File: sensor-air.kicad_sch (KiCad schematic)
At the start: 0 parts

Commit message: Adding I2C bus to circuit
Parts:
- added J7: Conn_02x04_Odd_Even, symbol Connector_Generic:Conn_02x04_Odd_Even
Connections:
- new net I2C.SCL: J7.6 (Pin_6)
- new net I2C.SDA: J7.8 (Pin_8)
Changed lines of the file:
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@@
 	(generator_version "8.0")
 	(paper "A4")
+	(bus_entry
+		(at 193.04 97.79)
+		(size 2.54 2.54)
+		(stroke
+			(width 0)
+			(type default)
+		)
+	)
+	(bus_entry
+		(at 193.04 100.33)
+		(size 2.54 2.54)
+		(stroke
+			(width 0)
+			(type default)
+		)
+	)
+	(wire
+		(pts
+			(xy 170.18 100.33) (xy 193.04 100.33)
+		)
+		(stroke
+			(width 0)
+			(type default)
+		)
+	)
+	(wire
+		(pts
+			(xy 170.18 97.79) (xy 193.04 97.79)
+		)
+		(stroke
+			(width 0)
+			(type default)
+		)
+	)
+	(bus
+		(pts
+			(xy 195.58 102.87) (xy 195.58 106.68)
+		)
+		(stroke
+			(width 0)
+			(type default)
+		)
+	)
+	(bus
+		(pts
+			(xy 195.58 106.68) (xy 214.63 106.68)
+		)
+		(stroke
+			(width 0)
+			(type default)
+		)
+	)
+	(bus
+		(pts
+			(xy 195.58 100.33) (xy 195.58 102.87)
+		)
+		(stroke
+			(width 0)
+			(type default)
+		)
+	)
+	(label "I2C.SCL"
+		(at 180.34 97.79 0)
+		(fields_autoplaced yes)
+		(effects
+			(font
+				(size 1.27 1.27)
+			)
+			(justify left bottom)
+		)
+	)
+	(label "I2C.SDA"
+		(at 180.34 100.33 0)
+		(fields_autoplaced yes)
+		(effects
+			(font
+				(size 1.27 1.27)
+			)
+			(justify left bottom)
+		)
+	)
+	(hierarchical_label "I2C{SCL SDA}"
+		(shape bidirectional)
+		(at 214.63 106.68 0)
+		(fields_autoplaced yes)
+		(effects
+			(font
+				(size 1.27 1.27)
+			)
+			(justify left)
+		)
+	)
+	(symbol
+		(lib_id "Connector_Generic:Conn_02x04_Odd_Even")
+		(at 162.56 95.25 0)
+		(unit 1)
+		(exclude_from_sim no)
+		(in_bom yes)
+		(on_board yes)
+		(dnp no)
+		(fields_autoplaced yes)
+		(property "Reference" "J7"
+			(at 163.83 86.36 0)
+			(effects
+				(font
+					(size 1.27 1.27)
+				)
+			)
+		)
+		(property "Value" "Conn_02x04_Odd_Even"
+			(at 163.83 88.9 0)
+			(effects
+				(font
+					(size 1.27 1.27)
+				)
+			)
+		)
+		(property "Footprint" ""
+			(at 162.56 95.25 0)
+			(effects
+				(font
+					(size 1.27 1.27)
+				)
+				(hide yes)
+			)
+		)
+		(property "Datasheet" "~"
+			(at 162.56 95.25 0)
+			(effects
+				(font
+					(size 1.27 1.27)
+				)
+				(hide yes)
+			)
+		)
+		(property "Description" "Generic connector, double row, 02x04, odd/even pin numbering scheme (row 1 odd numbers, row 2 even numbers), script generated (kicad-library-utils/schlib/autogen/connector/)"
+			(at 162.56 95.25 0)
+			(effects
+				(font
+					(size 1.27 1.27)
+				)
+				(hide yes)
+			)
+		)
+		(pin "3"
+		)
+		(pin "1"
+		)
+		(pin "5"
+		)
+		(pin "8"
+		)
+		(pin "7"
+		)
+		(pin "4"
+		)
+		(pin "2"
+		)
+		(pin "6"
+		)
+		(instances
+			(project ""
+				(path "/1c59de6a-87fe-4223-8898-4b0383164a31/51e979ab-bea6-4c65-a749-9f40ad447381"
+					(reference "J7")
+					(unit 1)
+				)
+			)
+		)
+	)
 )

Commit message: Adding symbols information
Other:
- company: (none) -> catbranchman
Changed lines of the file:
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@@
 	(generator_version "8.0")
 	(paper "A4")
+	(title_block
+		(company "catbranchman")
+		(comment 1 "Electrical Engineering Department")
+		(comment 2 "EE 156 / Stanford University")
+		(comment 3 "Flight Club, W6YX, Endurance")
+	)
 	(bus_entry
 		(at 193.04 97.79)

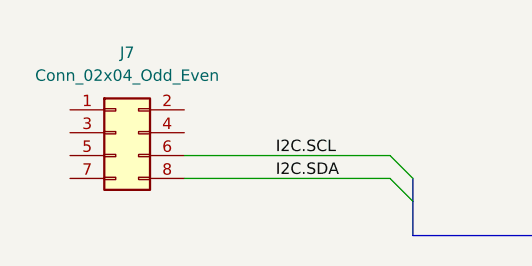
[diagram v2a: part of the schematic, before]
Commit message: Adding rest of schematic
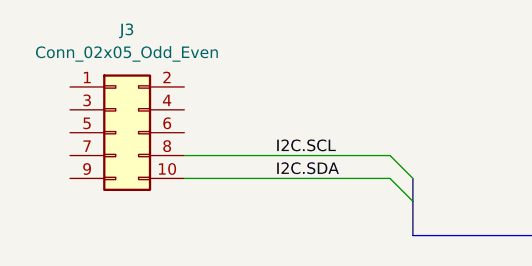
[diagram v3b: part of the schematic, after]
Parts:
- removed J7: Conn_02x04_Odd_Even, symbol Connector_Generic:Conn_02x04_Odd_Even
- added J3: Conn_02x05_Odd_Even, Connector_PinHeader_1.27mm:PinHeader_2x05_P1.27mm_Vertical_SMD, symbol Connector_Generic:Conn_02x05_Odd_Even
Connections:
- net I2C.SCL: now also J3.8 (Pin_8)
- net I2C.SDA: now also J3.10 (Pin_10)
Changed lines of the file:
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@@
 	)
 	(symbol
-		(lib_id "Connector_Generic:Conn_02x04_Odd_Even")
+		(lib_id "Connector_Generic:Conn_02x05_Odd_Even")
 		(at 162.56 95.25 0)
 		(unit 1)
@@
 		(dnp no)
 		(fields_autoplaced yes)
-		(property "Reference" "J7"
+		(property "Reference" "J3"
+			(at 163.83 83.82 0)
+			(effects
+				(font
+					(size 1.27 1.27)
+				)
+			)
+		)
+		(property "Value" "Conn_02x05_Odd_Even"
 			(at 163.83 86.36 0)
 			(effects
@@
 			)
 		)
-		(property "Value" "Conn_02x04_Odd_Even"
-			(at 163.83 88.9 0)
-			(effects
-				(font
-					(size 1.27 1.27)
-				)
-			)
-		)
-		(property "Footprint" ""
+		(property "Footprint" "Connector_PinHeader_1.27mm:PinHeader_2x05_P1.27mm_Vertical_SMD"
 			(at 162.56 95.25 0)
 			(effects
@@
 			)
 		)
-		(property "Datasheet" "~"
+		(property "Datasheet" "https://www.fischerelektronik.de/web_fischer/en_GB/VA/BLM2SMD10Z/datasheet.xhtml"
 			(at 162.56 95.25 0)
 			(effects
@@
 			)
 		)
-		(property "Description" "Generic connector, double row, 02x04, odd/even pin numbering scheme (row 1 odd numbers, row 2 even numbers), script generated (kicad-library-utils/schlib/autogen/connector/)"
+		(property "Description" "Generic connector, double row, 02x05, odd/even pin numbering scheme (row 1 odd numbers, row 2 even numbers), script generated (kicad-library-utils/schlib/autogen/connector/)"
 			(at 162.56 95.25 0)
 			(effects
@@
 			)
 		)
-		(pin "3"
+		(property "Mfr" "Fischer Elektronik"
+			(at 162.56 95.25 0)
+			(effects
+				(font
+					(size 1.27 1.27)
+				)
+				(hide yes)
+			)
 		)
-		(pin "1"
+		(property "Mfr P/N" "BLM 2 SMD 10 Z"
+			(at 162.56 95.25 0)
+			(effects
+				(font
+					(size 1.27 1.27)
+				)
+				(hide yes)
+			)
+		)
+		(property "Supplier_1" "Digikey"
+			(at 162.56 95.25 0)
+			(effects
+				(font
+					(size 1.27 1.27)
+				)
+				(hide yes)
+			)
+		)
+		(property "Supplier_1 P/N" "5496-BLM2SMD10Z-ND"
+			(at 162.56 95.25 0)
+			(effects
+				(font
+					(size 1.27 1.27)
+				)
+				(hide yes)
+			)
+		)
+		(property "Supplier_1 Unit Price" "$0.93000 "
+			(at 162.56 95.25 0)
+			(effects
+				(font
+					(size 1.27 1.27)
+				)
+				(hide yes)
+			)
+		)
+		(property "Supplier_1 Price @ Qty" ""
+			(at 162.56 95.25 0)
+			(effects
+				(font
+					(size 1.27 1.27)
+				)
+				(hide yes)
+			)
+		)
+		(property "Supplier_2" ""
+			(at 162.56 95.25 0)
+			(effects
+				(font
+					(size 1.27 1.27)
+				)
+				(hide yes)
+			)
+		)
+		(property "Supplier_2 P/N" ""
+			(at 162.56 95.25 0)
+			(effects
+				(font
+					(size 1.27 1.27)
+				)
+				(hide yes)
+			)
+		)
+		(property "Supplier_2 Unit Price" ""
+			(at 162.56 95.25 0)
+			(effects
+				(font
+					(size 1.27 1.27)
+				)
+				(hide yes)
+			)
+		)
+		(property "Supplier_2 Price @ Qty" ""
+			(at 162.56 95.25 0)
+			(effects
+				(font
+					(size 1.27 1.27)
+				)
+				(hide yes)
+			)
 		)
 		(pin "5"
+		)
+		(pin "4"
+		)
+		(pin "9"
+		)
+		(pin "3"
 		)
 		(pin "8"
@@
 		(pin "7"
 		)
-		(pin "4"
+		(pin "6"
+		)
+		(pin "1"
 		)
 		(pin "2"
 		)
-		(pin "6"
+		(pin "10"
 		)
 		(instances
 			(project ""
 				(path "/1c59de6a-87fe-4223-8898-4b0383164a31/51e979ab-bea6-4c65-a749-9f40ad447381"
-					(reference "J7")
+					(reference "J3")
 					(unit 1)
 				)

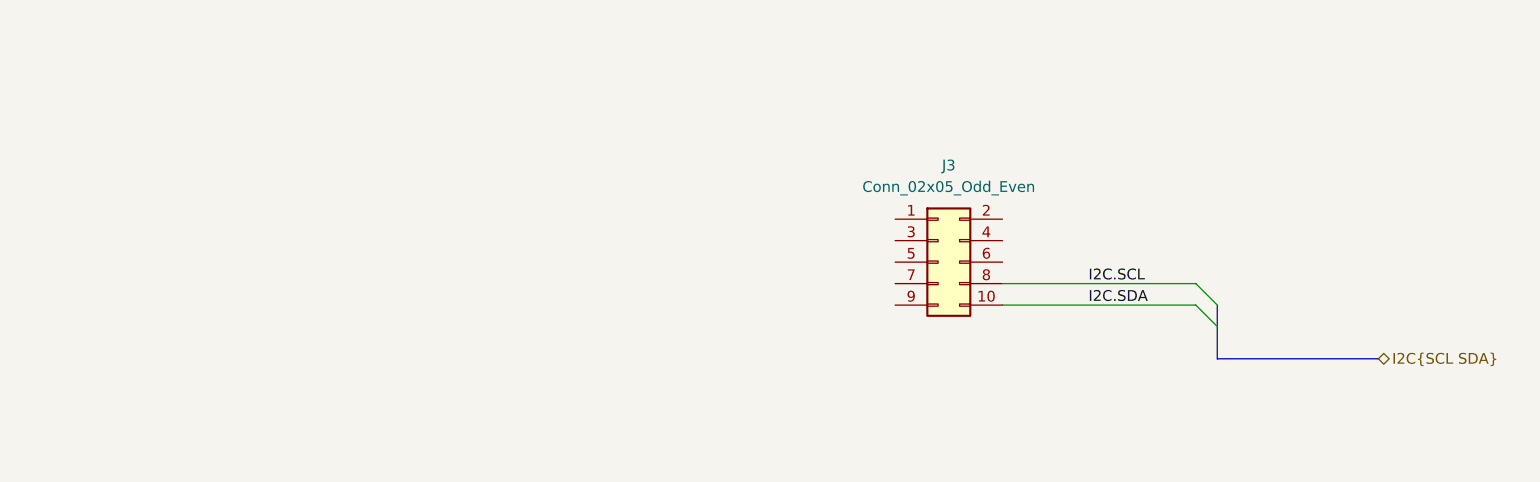
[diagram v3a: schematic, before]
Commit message: Spamming 0 ohm resistors
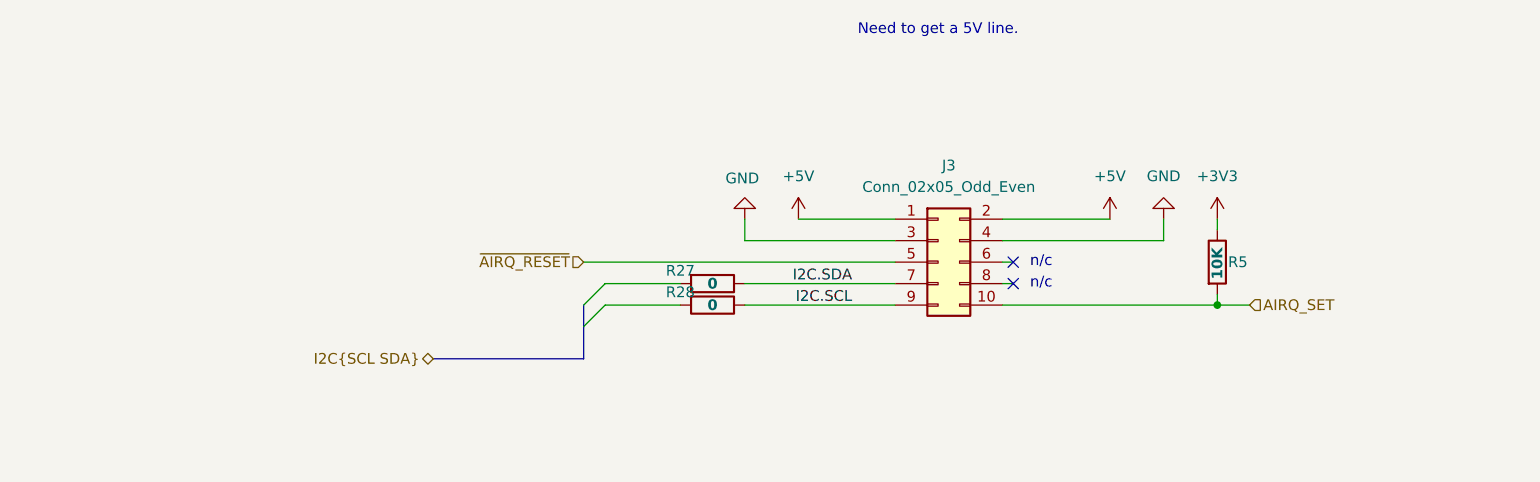
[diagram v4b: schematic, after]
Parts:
- added R27, R28: 0, Resistor_SMD:R_0603_1608Metric, symbol Device:R
- added R5: 10K, Resistor_SMD:R_0603_1608Metric, symbol Device:R
- J3: Mfr Fischer Elektronik -> Amphenol ICC (FCI); Mfr P/N BLM 2 SMD 10 Z -> 20021321-00010C4LF; Supplier_1 P/N 5496-BLM2SMD10Z-ND -> 609-3706-1-ND; Supplier_1 Price @ Qty (none) -> $0.79120; Supplier_1 Unit Price $0.93000 -> $1.35000
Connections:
- net I2C.SCL: now also J3.9 (Pin_9), R28.1; no longer J3.8 (Pin_8)
- net I2C.SDA: now also J3.7 (Pin_7), R27.1; no longer J3.10 (Pin_10)
- net +5V: now reaches J3.1 (Pin_1)
- net +5V: now also J3.2 (Pin_2)
- net GND: now reaches J3.3 (Pin_3)
- net GND: now also J3.4 (Pin_4)
- net ~{AIRQ_RESET}: now reaches J3.5 (Pin_5)
- new net +3V3: R5.1
- new net AIRQ_SET: J3.10 (Pin_10), R5.2
- no-connect marks 0 -> 2
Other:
- note added: "Need to get a 5V line."
- note added: "n/c"
- title: (none) -> Sensor - Air Quality

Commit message: Adding more 0 ohm resistors and pullups for I2C lines
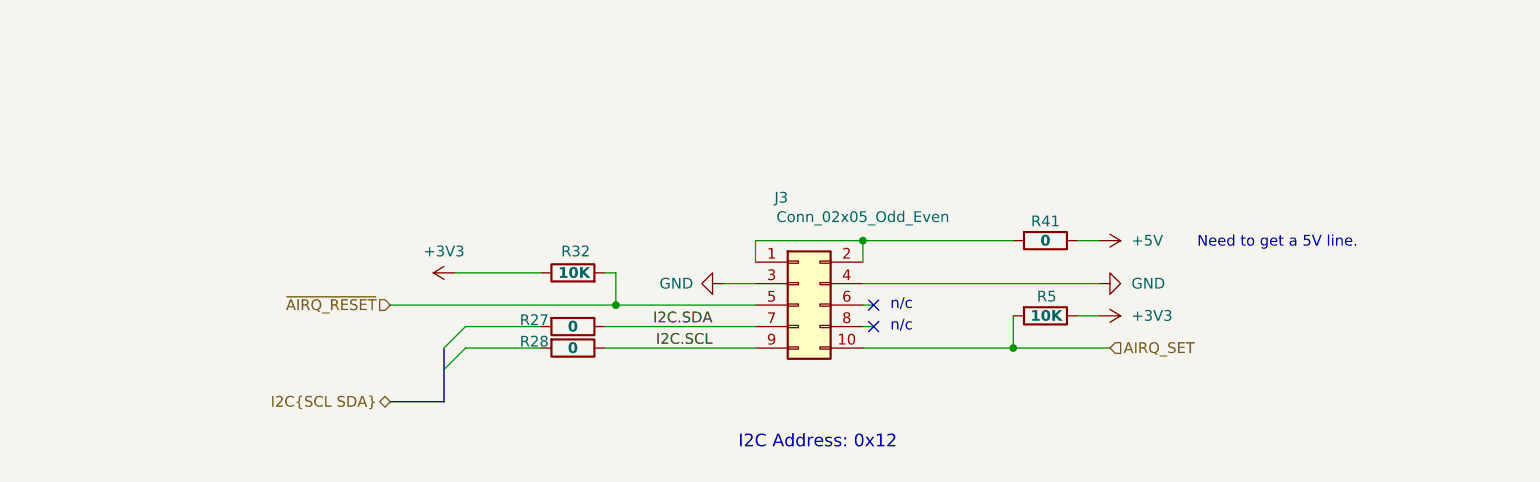
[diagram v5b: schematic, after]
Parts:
- added R32: 10K, Resistor_SMD:R_0603_1608Metric, symbol Device:R
- added R41: 0, Resistor_SMD:R_0603_1608Metric, symbol Device:R
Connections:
- net +3V3: now also R32.1
- net +5V: now also R41.1; no longer J3.1 (Pin_1), J3.2 (Pin_2)
- net ~{AIRQ_RESET}: now also R32.2
- new net: J3.1 (Pin_1), J3.2 (Pin_2), R41.2
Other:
- note added: "I2C Address: 0x12"
- moved on the sheet: J3, R27, R28, R5

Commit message: Adding diodes for Air Quality Sensor SET and RESET pins
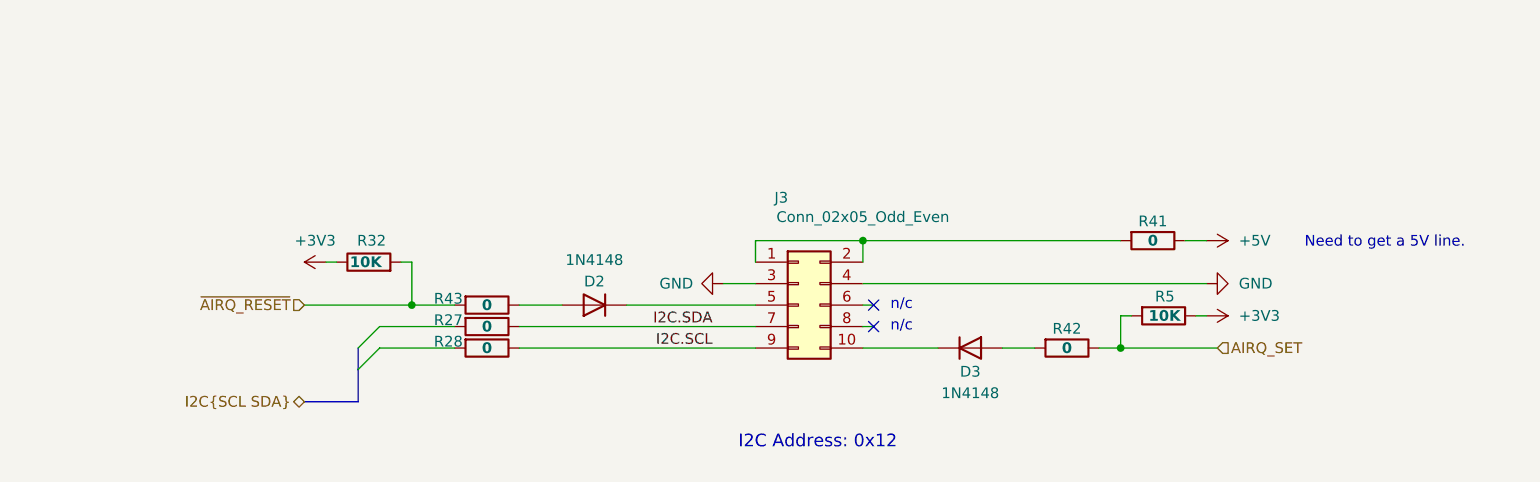
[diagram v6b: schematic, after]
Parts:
- added D2, D3: 1N4148, Diode_SMD:D_SOD-323F, symbol Device:D
- added R42, R43: 0, Resistor_SMD:R_0603_1608Metric, symbol Device:R
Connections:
- net AIRQ_SET: now also R42.1; no longer J3.10 (Pin_10)
- net ~{AIRQ_RESET}: now also R43.2; no longer J3.5 (Pin_5)
- new net: D2.2 (A), R43.1
- new net: D3.1 (K), J3.10 (Pin_10)
- new net: D3.2 (A), R42.2
- new net: D2.1 (K), J3.5 (Pin_5)
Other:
- moved on the sheet: R27, R28, R32, R41, R5

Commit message: Adding testpoints to I2C, SPI, and signals
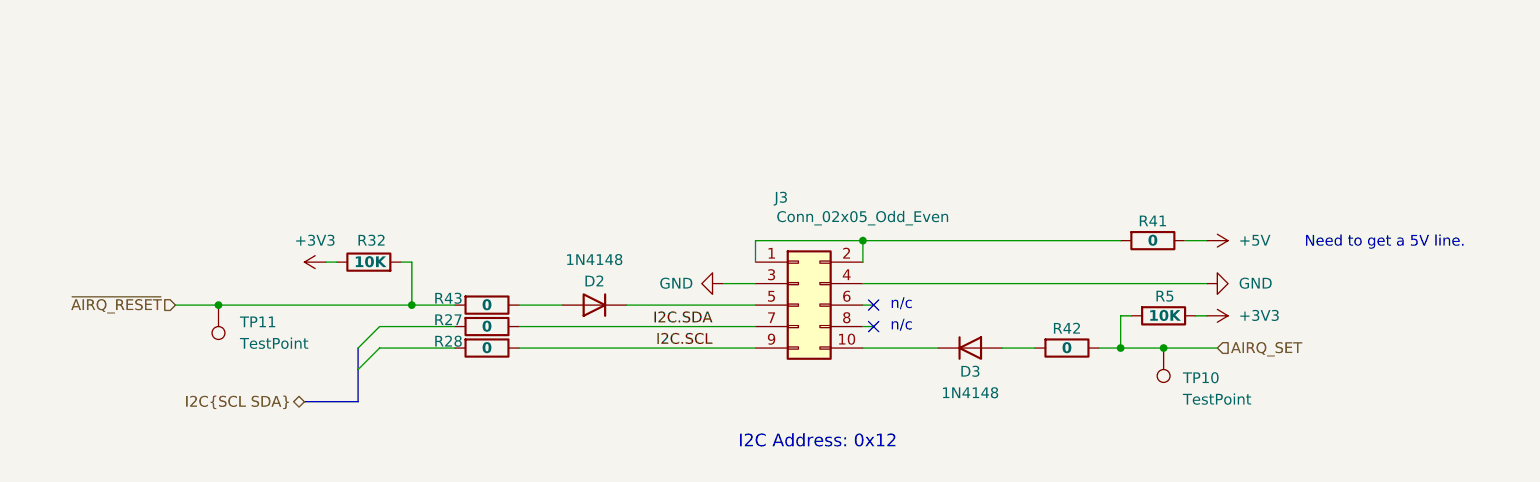
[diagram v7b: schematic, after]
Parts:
- added TP10, TP11: TestPoint, TestPoint:TestPoint_Loop_D2.50mm_Drill1.0mm, symbol Connector:TestPoint
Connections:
- net AIRQ_SET: now also TP10.1
- net ~{AIRQ_RESET}: now also TP11.1

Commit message: Fixing lots of ERC errors
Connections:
- net I2C.SCL: now also R28.2; no longer J3.9 (Pin_9), R28.1
- net I2C.SDA: now also R27.2; no longer J3.7 (Pin_7), R27.1
- new net: J3.9 (Pin_9), R28.1
- new net: J3.7 (Pin_7), R27.1
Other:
- moved on the sheet: D2, D3, J3, R27, R28, R32, R41, R42, R43, R5, TP10, TP11
